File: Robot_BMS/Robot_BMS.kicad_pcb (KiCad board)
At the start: 2 copper layers, 72.9 x 1 mm, 81 parts, among them IC1 STUSB4710AQTR, IC2 BQ76922RSNR, J1 632723300011, J2 Conn_01x14_Pin, J3 694108301002, J4 691137710002, Q1 2N7002, Q2 SIS413DN-T1-GE3, Q3 2N7002, Q4 SIS413DN-T1-GE3, U1 TPS54308DDCR, U2 LM3488MM, U3 CSD18563Q5A

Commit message: switching usb c pd chip to ap33772 due to better support online
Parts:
- added D2: 1N4750A, Diode_THT:D_DO-41_SOD81_P10.16mm_Horizontal, F.Cu at (368.7, 94.5)
- added D3: 1N4750A, Diode_THT:D_DO-41_SOD81_P10.16mm_Horizontal, F.Cu at (368.7, 85.7)
- added D4: 1N4750A, Diode_THT:D_DO-41_SOD81_P10.16mm_Horizontal, F.Cu at (368.7, 103.2)
- added F1: MF-LSMF500/16X-2, RobotBMS:FUSE_MF-LSMF185&slash_33X_BRN, B.Cu at (387.4, 41.5)
- added H1: MountingHole, MountingHole:MountingHole_3.2mm_M3, F.Cu at (170.5, 23.0)
- added H2: MountingHole, MountingHole:MountingHole_3.2mm_M3, F.Cu at (170.5, 117.8)
- added H3: MountingHole, MountingHole:MountingHole_3.2mm_M3, F.Cu at (70.4, 23.0)
- added H4: MountingHole, MountingHole:MountingHole_3.2mm_M3, F.Cu at (70.3, 117.8)
- added R26: 100k, RobotBMS:RES_R0603_ROM, B.Cu at (389.6, 97.9)
- added R27: 100k, RobotBMS:RES_R0603_ROM, B.Cu at (389.6, 89.1)
- added R28: 100k, RobotBMS:RES_R0603_ROM, B.Cu at (389.6, 106.6)
- C1, C10, C11, C12, C13, C14, C15, C16, C17, C18, C2, C20, C21, C22, C23, C24, C3, C4, C5, C6, C7, C8, C9, CR1, CR2, CR3, D1, IC1, IC2, L1, L2, Q1, Q2, Q3, Q4, R1, R10, R11, R12, R13, R14, R15, R16, R17, R18, R19, R2, R20, R21, R22, R23, R24, R25, R3, R4, R5, R6, R7, R8, R9, TP1, TP2, TP3, TP4, TP5, TP6, TP7, U1, U2, U3: moved to B.Cu
- TH1, TH2, TH3: value NTCLE100E3103HB0 -> 10K
- moved Q2 406.5 mm to (435.6, 41.3), turned to 180 degrees
- moved Q4 406.5 mm to (435.6, 47.4), turned to 180 degrees
- moved R10 396.3 mm to (430.4, 41.9), turned to 180 degrees
- moved R11 396.3 mm to (430.4, 44.3), turned to 180 degrees
- moved R12 396.3 mm to (430.4, 46.8), turned to 180 degrees
- moved R13 396.3 mm to (430.4, 49.2), turned to 180 degrees
- moved R9 396.3 mm to (430.4, 39.4), turned to 180 degrees
- moved C10 388.6 mm to (426.5, 42.1), turned to 180 degrees
- moved C11 388.6 mm to (426.5, 44.7), turned to 180 degrees
- moved C13 388.6 mm to (426.5, 47.3), turned to 180 degrees
- moved C9 388.6 mm to (426.5, 39.5), turned to 180 degrees
- moved R19 387.0 mm to (425.7, 79.1), turned to 180 degrees
- moved R25 386.7 mm to (425.6, 76.6), turned to 180 degrees
- moved C22 385.3 mm to (424.9, 74.1), turned to 180 degrees
- moved R14 380.5 mm to (422.4, 39.5), turned to 180 degrees
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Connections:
- Q4 pad 1: /Battery Management/TO_LOAD -> Net-(Q4-S_1)
- Q4 pad 2: /Battery Management/TO_LOAD -> Net-(Q4-S_1)
- Q4 pad 3: /Battery Management/TO_LOAD -> Net-(Q4-S_1)
- R14 pad 1: Net-(IC2-SRP) -> GND
- R14 pad 2: GND -> Net-(IC2-SRP)
- R17 pad 2: /Battery Management/TO_LOAD -> Net-(Q4-S_1)
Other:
- board size 72.9 x 1 mm -> 108.6 x 103.7 mm
- copper layers 2 -> 4

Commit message: placed connectors for BMS PCB
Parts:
- removed B1, B2, B3: BH-18650-PC, RobotBMS:BAT_BH-18650-PC_MPD
- added BT1: BK-18650-CLIP, RobotBMS:BAT_BK-18650-CLIP, F.Cu at (368.1, -19.7)
- added BT2: BK-18650-CLIP, RobotBMS:BAT_BK-18650-CLIP, F.Cu at (382.6, -19.7)
- added BT3: BK-18650-CLIP, RobotBMS:BAT_BK-18650-CLIP, F.Cu at (397.1, -19.7)
- added BT4: BK-18650-CLIP, RobotBMS:BAT_BK-18650-CLIP, F.Cu at (411.6, -19.7)
- added BT5: BK-18650-CLIP, RobotBMS:BAT_BK-18650-CLIP, F.Cu at (426.1, -19.7)
- added BT6: BK-18650-CLIP, RobotBMS:BAT_BK-18650-CLIP, F.Cu at (440.6, -19.7)
- added C4: 10u, RobotBMS:CAPC1608X90N, F.Cu at (366.3, 10.2)
- added C5: 0.1u, RobotBMS:CAPC17595_87N_KEM, F.Cu at (376.6, 7.66)
- added C6: 1u, RobotBMS:CAP_1608_TDK, F.Cu at (377.5, -6.32)
- added C7: 0.1u, RobotBMS:CAPC17595_87N_KEM, F.Cu at (376.6, 10.3)
- added C8: 1u, RobotBMS:CAP_1608_TDK, F.Cu at (377.5, -3.77)
- added IC1: AP33772DKZ-13, RobotBMS:QFN50P400X400X80-25N-D, F.Cu at (373.8, 3.21)
- added LED1: SML-D12V8WT86, RobotBMS:SMLD12V8WT86, F.Cu at (372.6, 9.13)
- added Q2: NDT3055L, Package_TO_SOT_SMD:SOT-223-3_TabPin2, F.Cu at (365.7, -3.40)
- added Q3: NDT3055L, Package_TO_SOT_SMD:SOT-223-3_TabPin2, F.Cu at (365.7, 4.93)
- added R10: 5k1, RobotBMS:ERA3AEB101V, F.Cu at (372.7, -1.22)
- added R33: 10k, RobotBMS:RC0603N_YAG, F.Cu at (335.7, 45.3)
- added R34: 10k, RobotBMS:RC0603N_YAG, F.Cu at (335.7, 47.7)
- added R6: 10k, RobotBMS:RC0603N_YAG, F.Cu at (376.8, -1.27)
- added R7: 10 milli_ohm, RobotBMS:RESC1608X60N, F.Cu at (372.7, -6.32)
- added R8: 1k, RobotBMS:RES_V0603_VIS, F.Cu at (362.7, 10.4)
- added R9: 5k1, RobotBMS:ERA3AEB101V, F.Cu at (372.7, -3.77)
- added RT1: 10k, RobotBMS:THRMC0603X33N, F.Cu at (378.5, 1.03)
- renumbered C7 to C10, C8 to C11, C9 to C12, C10 to C13, C11 to C14, C12 to C15, C13 to C16, C14 to C17, C15 to C18, C16 to C19, C17 to C20, C18 to C21, C19 to C22, C20 to C23, C21 to C24, C22 to C25, C23 to C26, C24 to C27, C6 to C9, D2 to D1, D3 to D2, D4 to D3, D1 to D4, H2 to H1, H3 to H2, H4 to H3, H1 to H4, Q2 to Q4, Q3 to Q5, Q4 to Q6, R7 to R11, R8 to R12, R26 to R13, R9 to R14, R10 to R15, R11 to R16, R12 to R17, R13 to R18, R14 to R19, R15 to R20, R16 to R21, R17 to R22, R18 to R23, R27 to R24, R28 to R25, R19 to R26, R20 to R27, R21 to R28, R22 to R29, R23 to R30, R24 to R31, R25 to R32
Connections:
- CR1 pad 1: VBUS -> /Charging Circuit/USB_C
- IC2 pad 28: unconnected-(IC2-LD-Pad28) -> /Battery Management/LD
- J2 pad 1: unconnected-(J2-Pin_1-Pad1) -> /To MCU OR System/USB_C_Interrupt

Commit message: Battery holders placed for 18650 fit
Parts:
- added J3: S6B-PH-K-S_LF__SN_, RobotBMS:JST_S6B-PH-K-S_LF__SN_, F.Cu at (493.5, 53.0)
- added J4: S6B-PH-K-S_LF__SN_, RobotBMS:JST_S6B-PH-K-S_LF__SN_, F.Cu at (493.5, 62.2)
- J2: value Conn_01x14_Pin -> 39-30-0040; footprint Connector_PinHeader_2.54mm:PinHeader_1x14_P2.54mm_Vertical -> RobotBMS:39-30-Y040
- moved BT6 364.9 mm to (94.3, 95.3), turned to 180 degrees
- moved BT5 330.4 mm to (94.3, 72.5), turned to 180 degrees
- moved BT3 302.5 mm to (146.3, 95.3)
- moved BT4 282.4 mm to (94.3, 49.8), turned to 180 degrees
- moved BT2 267.2 mm to (146.3, 72.5)
- moved BT1 246.3 mm to (146.2, 49.8)
- moved J2 34.8 mm to (125.2, 113.0), turned to 0 degrees
- moved C10 15.5 mm to (396.8, 46.8)
- moved C11 15.5 mm to (402.3, 48.1)
- moved C12 15.5 mm to (411.2, 41.8)
- moved C13 15.5 mm to (411.2, 44.4)
- moved C14 15.5 mm to (411.2, 47.0)
- moved C15 15.5 mm to (396.1, 41.8)
- moved C16 15.5 mm to (411.2, 49.6)
- moved C17 15.5 mm to (396.8, 49.4)
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- renumbered BT2 to BT1, BT3 to BT2, BT5 to BT3, BT1 to BT4, BT4 to BT5, J3 to J5, J4 to J6, R34 to R22, R22 to R23, R23 to R24, R33 to R25, R24 to R26, R25 to R27, R26 to R28, R27 to R29, R28 to R30, R29 to R31, R30 to R32, R31 to R33, R32 to R34
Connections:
- J2 pad 1: /To MCU OR System/USB_C_Interrupt -> GND
- J2 pad 3: /Thermistors/ADC3_MCU -> /Battery Management/TO_LOAD
- J2 pad 4: /Thermistors/ADC2_MCU -> /Battery Management/TO_LOAD

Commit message: adding qwik connectors replacing old jst ph 6 pin ones
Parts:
- added ?: , clipboard:29777afd-4317-4b21-83d4-984304780fb8, F.Cu at (123.4, 32.0)
- C22, C4, C5, C6, C7, C8, IC1, LED1, Q2, Q3, R10, R22, R25, R6, R7, R8, R9, RT1, TH1, TH2, TH3: moved to B.Cu
- moved J4 401.6 mm to (95.4, 115.0)
- moved J3 386.1 mm to (112.5, 115.1)
- moved C25 356.2 mm to (70.2, 41.2), turned to -90 degrees
- moved R34 354.7 mm to (72.7, 40.5), turned to -90 degrees
- moved R28 352.7 mm to (75.1, 40.4), turned to -90 degrees
- moved R29 348.5 mm to (71.7, 47.1), turned to -90 degrees
- moved R32 346.2 mm to (74.2, 47.1), turned to -90 degrees
- moved C23 339.7 mm to (76.5, 51.3), turned to -90 degrees
- moved C20 335.1 mm to (76.4, 55.5), turned to -90 degrees
- moved C24 334.4 mm to (79.4, 21.1)
- moved C26 334.4 mm to (78.9, 23.8)
- moved C27 334.4 mm to (78.9, 26.1)
- moved C4 332.3 mm to (108.8, 91.3)
- moved C5 332.3 mm to (108.8, 93.9)
- moved C9 332.3 mm to (109.8, 96.3)
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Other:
- board text added: "CONNECTOR_1"
- board text added: "CONNECTOR_2"
- board text added: "DC PWR"
- board text added: "PWR CONNECTOR"
- board text added: "ROBOTICS"
- board text added: "SOLAR PWR"
- board text added: "USB-C PWR"
- board text added: "VELION"

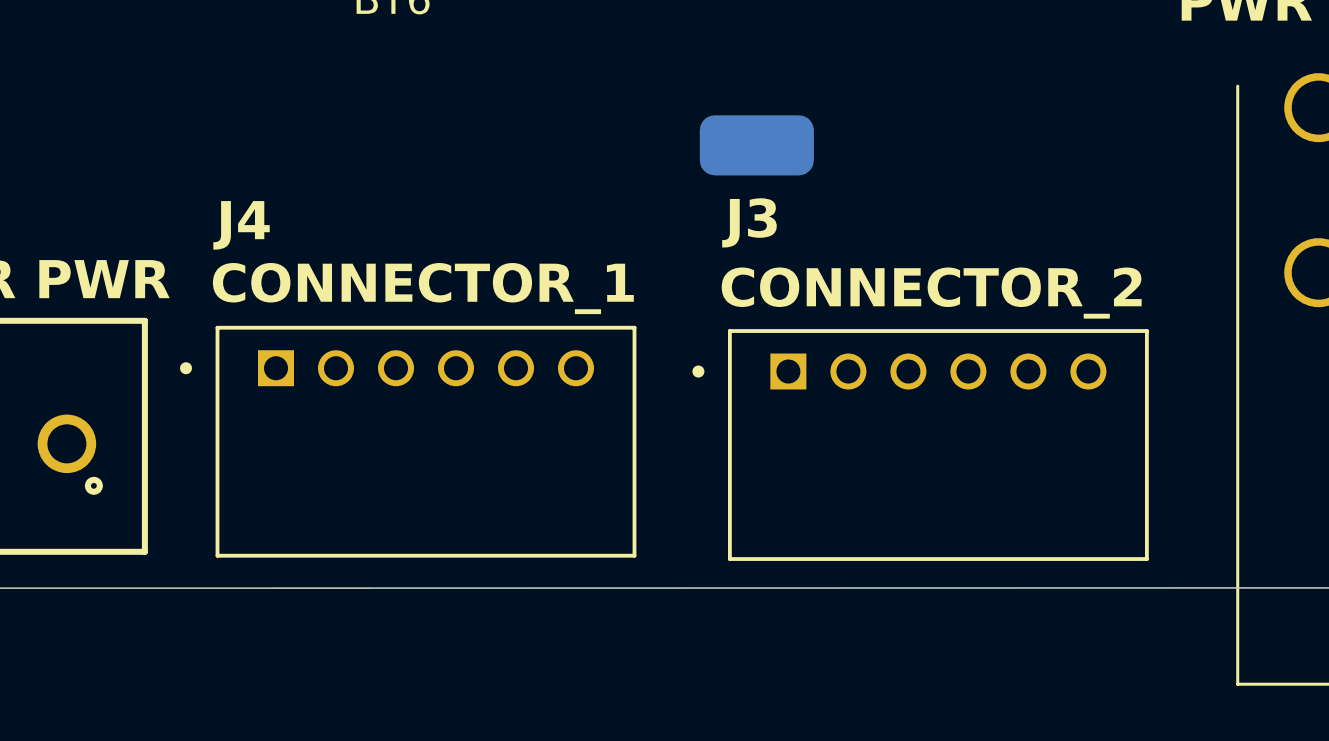
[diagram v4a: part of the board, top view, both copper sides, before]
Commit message: qwikk connector 3d model and footprint in RobotBMS
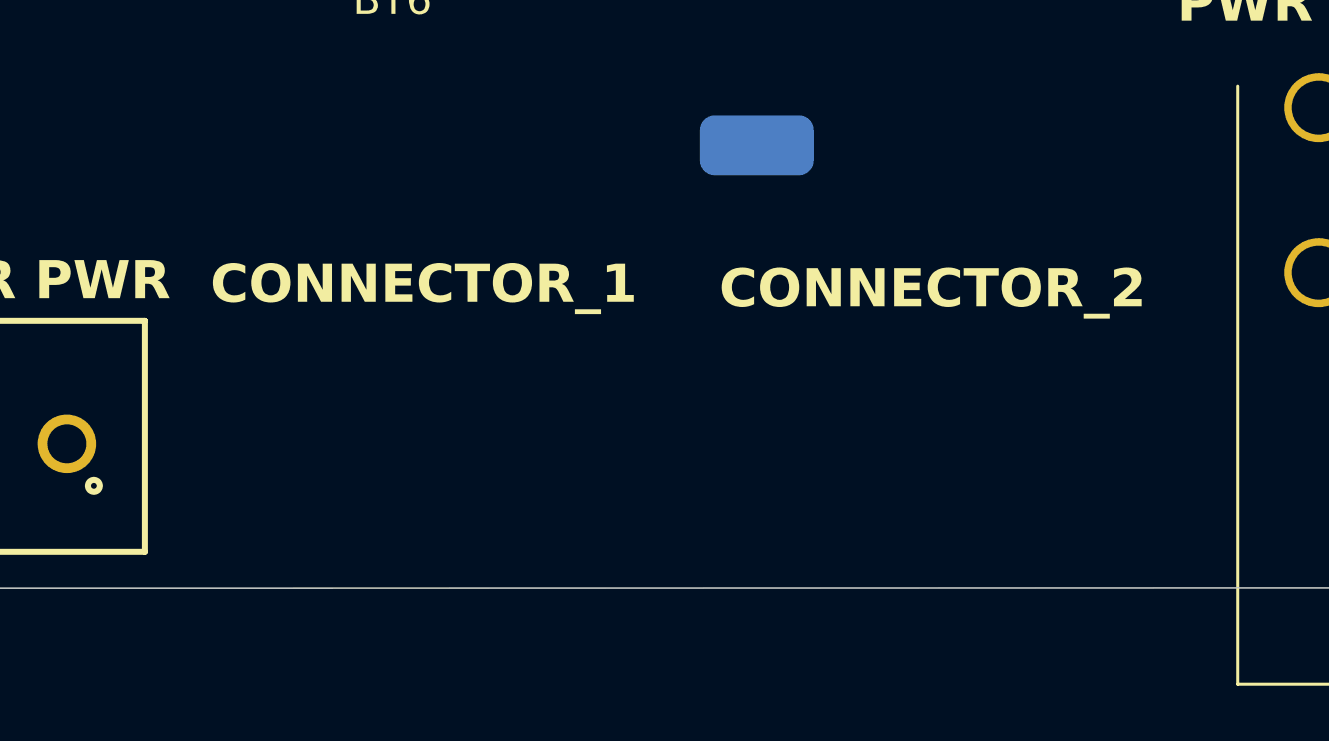
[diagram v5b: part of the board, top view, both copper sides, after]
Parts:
- removed J3, J4: S6B-PH-K-S_LF__SN_, RobotBMS:JST_S6B-PH-K-S_LF__SN_
